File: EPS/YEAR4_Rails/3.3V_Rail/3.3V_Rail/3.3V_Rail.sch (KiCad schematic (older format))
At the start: 20 parts

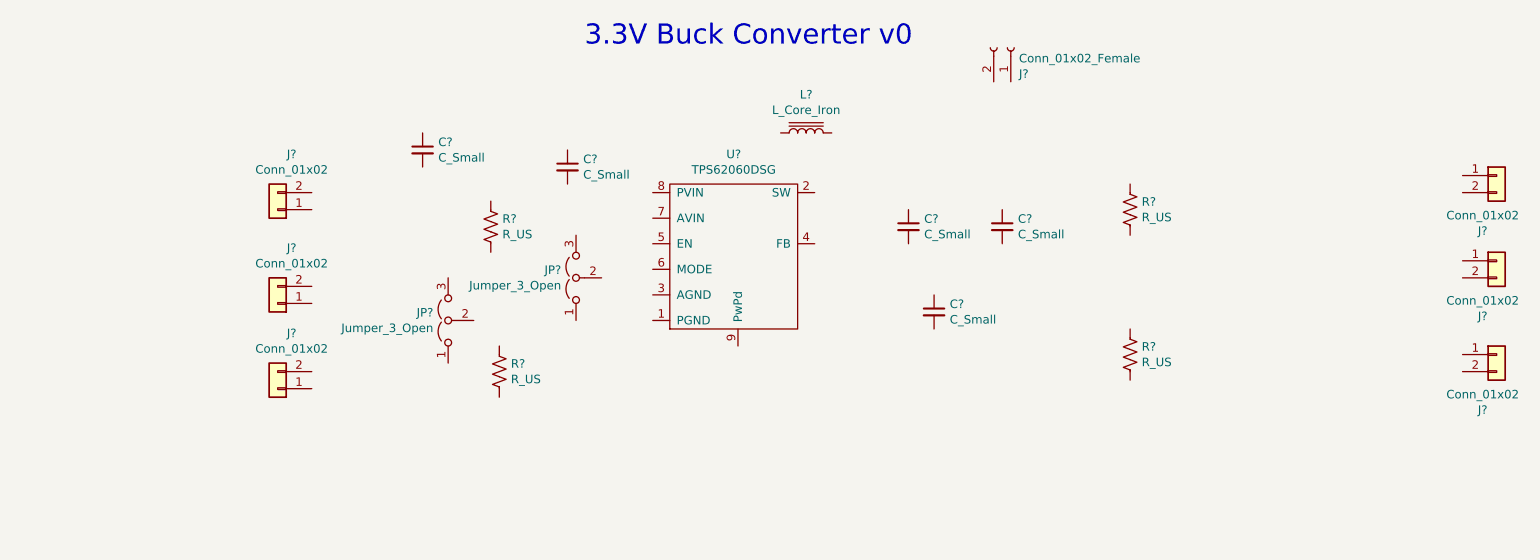
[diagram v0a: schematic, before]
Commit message: 3.3V rail
Schematic v.0.1
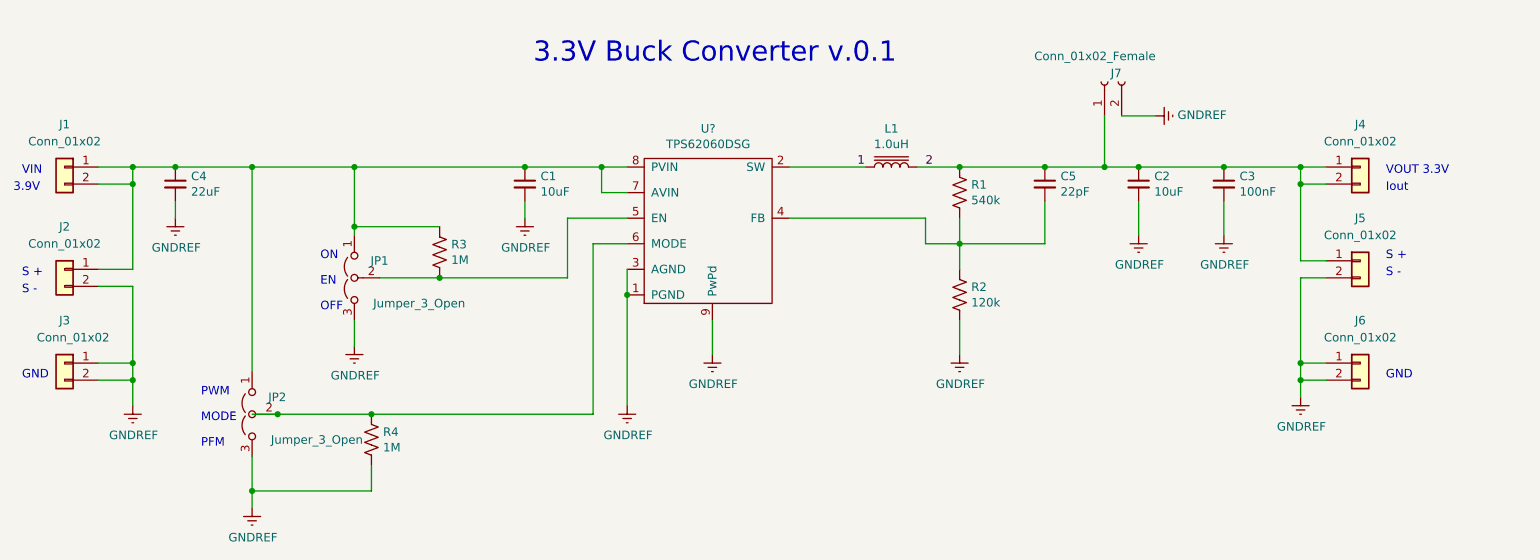
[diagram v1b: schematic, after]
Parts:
- C1, C2: renamed from C?; value C_Small -> 10uF
- C3: renamed from C?; value C_Small -> 100nF
- C4: renamed from C?; value C_Small -> 22uF
- C5: renamed from C?; value C_Small -> 22pF
- L1: renamed from L?; value L_Core_Iron -> 1.0uH
- R1: renamed from R?; value R_US -> 540k
- R2: renamed from R?; value R_US -> 120k
- R3, R4: renamed from R?; value R_US -> 1M
- gave numbers to parts that had none: 9
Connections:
- net 2: now reaches J7.1 (Pin_1)
- net 2: now also C2.1, C3.1, C5.1, J4.1 (Pin_1), J4.2 (Pin_2), J5.1 (Pin_1), L1.2, R1.1
- net GNDREF: now reaches J7.2 (Pin_2)
- net GNDREF: now also C1.2, C2.2, C3.2, C4.2, J2.2 (Pin_2), J3.1 (Pin_1), J3.2 (Pin_2), J5.2 (Pin_2), J6.1 (Pin_1), J6.2 (Pin_2), JP1.3 (B), JP2.3 (B), R2.2, R4.2, U?.1 (PGND), U?.3 (AGND), U?.9 (PwPd)
- net at R3.1: now also C1.1, C4.1, J1.1 (Pin_1), J1.2 (Pin_2), J2.1 (Pin_1), JP1.1 (A), JP2.1 (A), U?.7 (AVIN), U?.8 (PVIN)
- net at R3.2: now also JP1.2 (C), U?.5 (EN)
- net at R4.1: now also JP2.2 (C), U?.6 (MODE)
- net 1: now reaches U?.2 (SW)
- net 1: now also L1.1
- net at U?.4 (FB): now also C5.2, R1.2, R2.1
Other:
- note added: "3.3V Buck Converter v.0.1"
- note added: "3.9V"
- note added: "EN"
- note added: "GND"
- note added: "GND\n"
- note added: "Iout"
- note added: "MODE"
- note added: "OFF"
- note added: "ON"
- note added: "PFM"
- note added: "PWM"
- note added: "S +"
- note added: "S -"
- note added: "S -\n"
- note added: "VIN"
- note added: "VOUT 3.3V"
- note removed: "3.3V Buck Converter v0"
- moved on the sheet: C1, C2, C3, C4, C5, J1, J2, J3, J4, J5, J6, J7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

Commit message: Update 3.3V_Rail.sch
Update v.0.1
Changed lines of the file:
@@
 	2500 2400 3100 2400
-Wire Wire Line
-	2500 3850 2650 3850
-Connection ~ 2650 3850
 Wire Wire Line
 	2650 3850 3200 3850
